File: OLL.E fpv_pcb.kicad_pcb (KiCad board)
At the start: 2 copper layers, 122 parts, among them J10 Conn_01x05_Pin, J2 RC, J3 Conn_01x02_Pin, J7 m4 rear left, J8 reciver, J9 TYPE-C-31-M-12, M1 M1 front left, M2 M2 front right, M3 M3 rear right, Q1 2N7002, U1 MP2315GJ, U10 AON7410, U11 UCC27511ADBV, U12 AON7410, U13 BMP280, U14 STM32H753VITx, U15 USBLC6-2SC6, U2 W25Q128JVSIQ, U3 MP2315GJ, U4 ICM-42688-P, U5 UCC27511ADBV, U6 ul_AON7410, U7 UCC27511ADBV, U8 AON7410, U9 UCC27511ADBV, Y2 8HMz

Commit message: update sd card
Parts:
- removed C13: 100nf, Capacitor_SMD:C_0603_1608Metric
- removed R7: 10k, Resistor_SMD:R_0603_1608Metric
- removed U2: W25Q128JVSIQ, Package_SO:SOIC-8-1EP_3.9x4.9mm_P1.27mm_EP2.29x3mm
- added C47: 100nF, Capacitor_SMD:C_0603_1608Metric, B.Cu at (253.1, 64.9)
- added C48: 10uF, Capacitor_SMD:C_0603_1608Metric, B.Cu at (251.3, 61.4)
- added J1: Micro_SD_Card, Connector_Card:microSD_HC_Hirose_DM3D-SF, B.Cu at (241.7, 69.7)
- added R28: 47k, Resistor_SMD:R_0603_1608Metric, B.Cu at (251.4, 67.5)
- added R29: 47k, Resistor_SMD:R_0603_1608Metric, B.Cu at (249.6, 67.4)
- added R30: 47k, Resistor_SMD:R_0603_1608Metric, B.Cu at (249.6, 64.3)
- added R31: 47k, Resistor_SMD:R_0603_1608Metric, B.Cu at (253.1, 61.4)
- added R32: 47k, Resistor_SMD:R_0603_1608Metric, B.Cu at (250.2, 69.8)
- added REF**: WEEE-Logo_4.2x6mm_SilkScreen, Symbol:WEEE-Logo_4.2x6mm_SilkScreen, F.Cu at (251.9, 43.3)
- added REF**: LayerMarker_2_3.81x2.54mm_TextH1mm_P1.27mm_Named, Symbol:LayerMarker_2_3.81x2.54mm_TextH1mm_P1.27mm_Named, F.Cu at (246.8, 43.3)
- added REF**: OSHW-Symbol_6.7x6mm_SilkScreen, Symbol:OSHW-Symbol_6.7x6mm_SilkScreen, B.Cu at (229.5, 55.0)
- D8, LS1: moved to B.Cu
- moved R27 102.0 mm to (253.1, 61.6), turned to 90 degrees
- moved R26 101.8 mm to (253.0, 58.4), turned to 90 degrees
- moved Q1 96.8 mm to (251.5, 65.1)
- moved D7 93.1 mm to (251.4, 68.4)
- moved LS1 81.2 mm to (228.2, 68.5), turned to 180 degrees
- moved C46 72.4 mm to (211.3, 56.7), turned to 90 degrees
- moved R24 72.4 mm to (224.3, 44.0), turned to 180 degrees
- moved C45 69.7 mm to (208.4, 56.0), turned to 180 degrees
- moved J9 63.9 mm to (209.7, 46.4), turned to -90 degrees
- moved R23 61.2 mm to (213.2, 40.4)
- moved D8 45.8 mm to (210.4, 53.4), turned to 180 degrees
- moved U15 45.8 mm to (209.1, 53.4)
- moved D6 41.5 mm to (219.7, 68.1), turned to 90 degrees
- moved M2 35.5 mm to (208.5, 59.2)
- moved U11 31.4 mm to (214.6, 68.6)
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- renumbered J7 to M2, M2 to M3, M3 to M4, J3 to j3
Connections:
- D6 pad 1: (no net) -> +VBAT
- D6 pad 2: (no net) -> Net-(C29--)
- LS1 pad 1: (no net) -> +5V_FC
- LS1 pad 2: (no net) -> GND
- U14 pad 51: CS_FLASH -> unconnected-(U14-PB12-Pad51)
- U14 pad 65: unconnected-(U14-PC8-Pad65) -> C1_D0
- U14 pad 66: unconnected-(U14-PC9-Pad66) -> C1_D1
- U14 pad 78: unconnected-(U14-PC10-Pad78) -> C1_D2
- U14 pad 79: unconnected-(U14-PC11-Pad79) -> C1_D3
- U14 pad 80: unconnected-(U14-PC12-Pad80) -> CLK
- U14 pad 83: unconnected-(U14-PD2-Pad83) -> CMD
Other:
- board outline added: 47.6 x 41.5 mm

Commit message: update IMU
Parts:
- removed JP1: Jumper_2_Open, Jumper:SolderJumper-2_P1.3mm_Open_RoundedPad1.0x1.5mm
- added SW1: SW_SPST, Button_Switch_SMD:SW_SPST_B3U-1000P, F.Cu at (243.3, 41.1)
- added SW2: SW_SPST, Button_Switch_SMD:SW_SPST_B3U-1000P, F.Cu at (246.9, 41.1)
- moved REF** 4.20 mm to (250.9, 42.9), turned to 90 degrees
- moved J1 0.77 mm to (241.2, 70.2)
- moved D8 0.64 mm to (210.8, 53.9)
- turned R5 to 180 degrees
- turned Y2 to 0 degrees
- renumbered j3 to BAT
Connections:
- D3 pad 1: +VBAT -> (no net)
- D3 pad 2: Net-(C26--) -> (no net)
- D4 pad 1: +VBAT -> (no net)
- D4 pad 2: Net-(C27--) -> (no net)
- D5 pad 1: +VBAT -> (no net)
- D5 pad 2: Net-(C28--) -> (no net)
- D6 pad 1: +VBAT -> (no net)
- D6 pad 2: Net-(C29--) -> (no net)
- LS1 pad 1: +5V_FC -> (no net)
- LS1 pad 2: GND -> (no net)
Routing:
- net GND: track 0.00 -> 75.3 mm, vias 0 -> 7
- net +VBAT: track 0.00 -> 56.9 mm, vias 0 -> 5
- net +3V3_FC: track 0.00 -> 21.2 mm, vias 0 -> 3
- net VDDA_FILT: track 0.00 -> 13.1 mm
- net Net-(C43-+): track 0.00 -> 12.8 mm, vias 0 -> 2
- net Net-(C42-+): track 0.00 -> 9.72 mm, vias 0 -> 2
- net GYRO_INT: track 0.00 -> 9.60 mm
- net BOOT0: track 0.00 -> 9.35 mm
- net ADC_VBAT: track 0.00 -> 9.10 mm
- net Net-(C18--): track 0.00 -> 9.08 mm, vias 0 -> 3
- net Net-(C19-+): track 0.00 -> 8.66 mm, vias 0 -> 2
- net Net-(R8-+): track 0.00 -> 7.97 mm
- net Net-(C18-+): track 0.00 -> 5.75 mm, vias 0 -> 2
- net SPI1_SDO: track 0.00 -> 3.95 mm
- net SPI1_SDI: track 0.00 -> 3.82 mm
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- added copper zone on F.Cu, net +3V3_FC
- added copper zone on F.Cu, net +3V3_IMU
- added copper zone on B.Cu, net GND
- added copper zone on F.Cu, net GND
- added copper zone on In1.Cu, net GND
- added copper zone on In4.Cu, net GND
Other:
- copper layers 2 -> 6

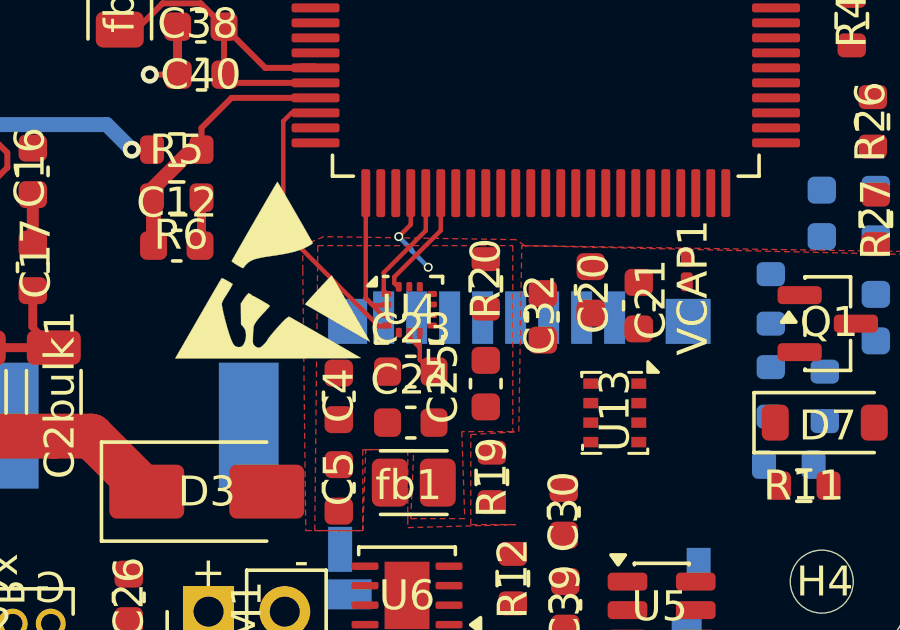
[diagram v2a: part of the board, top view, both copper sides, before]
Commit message: fix imu wire connection
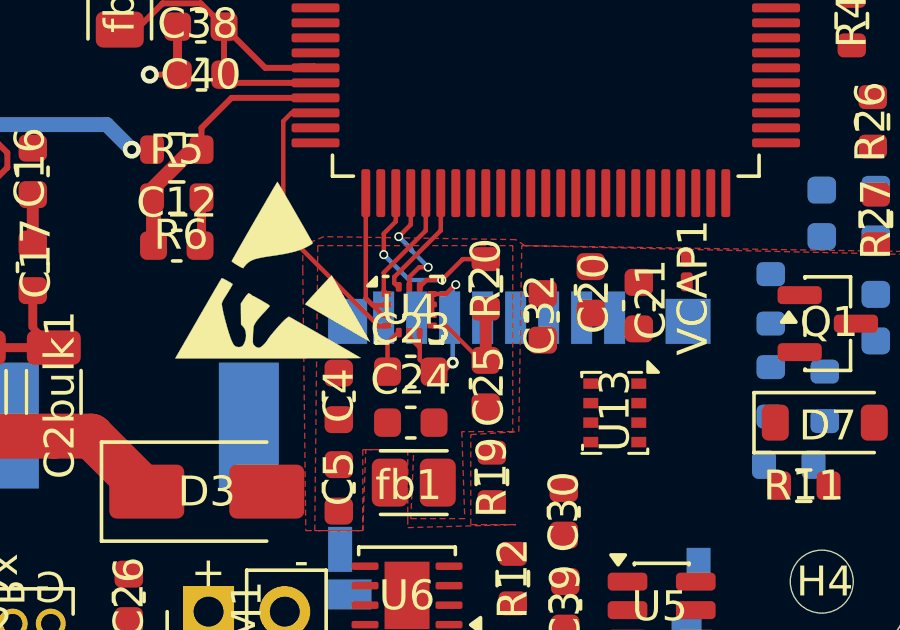
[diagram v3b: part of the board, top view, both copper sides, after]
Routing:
- net GYRO_CS: track 0.00 -> 7.07 mm, vias 0 -> 2
- net +3V3_IMU: track 0.00 -> 5.44 mm
- net GND: track 75.3 -> 80.2 mm, vias 7 -> 9
- net SPI1_SCK: track 3.04 -> 4.14 mm
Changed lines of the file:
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@@
 		(tags "capacitor")
 		(property "Reference" "C25"
-			(at 0 -1.43 90)
+			(at -0.1 0.1 90)
 			(layer "F.SilkS")
 			(effects
@@
 	)
 	(segment
+		(start 238.375 66.7)
+		(end 238.7 66.7)
+		(width 0.15)
+		(layer "F.Cu")
+		(net 1)
+	)
+	(segment
 		(start 220.8 63.5)
 		(end 222.3 65)
@@
 	)
 	(segment
+		(start 238.3125 64.1125)
+		(end 238.3125 64.7875)
+		(width 0.15)
+		(layer "F.Cu")
+		(net 1)
+	)
+	(segment
 		(start 226.5 47.3)
 		(end 226.5 46.5)
@@
 	)
 	(segment
+		(start 238.7 66.7)
+		(end 239 66.4)
+		(width 0.15)
+		(layer "F.Cu")
+		(net 1)
+	)
+	(segment
 		(start 237.9 66.3)
 		(end 237.9 65.9)
@@
 	)
 	(segment
+		(start 238.769671 64.1125)
+		(end 239.041086 63.841085)
+		(width 0.15)
+		(layer "F.Cu")
+		(net 1)
+	)
+	(segment
 		(start 236.6 43.675)
 		(end 236.6 45.4)
@@
 	)
 	(segment
+		(start 238.3125 64.1125)
+		(end 238.769671 64.1125)
+		(width 0.15)
+		(layer "F.Cu")
+		(net 1)
+	)
+	(segment
 		(start 236.633968 64.7875)
 		(end 236.7875 64.7875)
@@
 	)
 	(via
+		(at 239 66.4)
+		(size 0.4)
+		(drill 0.2)
+		(layers "F.Cu" "B.Cu")
+		(net 1)
+	)
+	(via
 		(at 226.5 46.5)
 		(size 0.6)
@@
 	)
 	(via
+		(at 239.1 63.8)
+		(size 0.3)
+		(drill 0.2)
+		(layers "F.Cu" "B.Cu")
+		(net 1)
+	)
+	(via
 		(at 226.2 39.9)
 		(size 0.6)
@@
 	)
 	(segment
+		(start 239 66.4)
+		(end 239 63.9)
+		(width 0.15)
+		(layer "B.Cu")
+		(net 1)
+	)
+	(segment
 		(start 226.2 39.9)
 		(end 225.4 39.9)
@@
 	)
 	(segment
+		(start 239 63.9)
+		(end 239.1 63.8)
+		(width 0.15)
+		(layer "B.Cu")
+		(net 1)
+	)
+	(segment
 		(start 221.5 65.8)
 		(end 222.3 65)
@@
 	)
 	(segment
+		(start 240.1 66.325)
+		(end 239.925 66.325)
+		(width 0.4)
+		(layer "F.Cu")
+		(net 4)
+	)
+	(segment
+		(start 238.35 65.2)
+		(end 238.3125 65.1625)
+		(width 0.1)
+		(layer "F.Cu")
+		(net 4)
+	)
+	(segment
+		(start 238.8 65.2)
+		(end 238.35 65.2)
+		(width 0.14)
+		(layer "F.Cu")
+		(net 4)
+	)
+	(segment
+		(start 240.1 64.6)
+		(end 240.1 66.325)
+		(width 0.4)
+		(layer "F.Cu")
+		(net 4)
+	)
+	(segment
+		(start 236.825 66.7)
+		(end 236.825 65.75)
+		(width 0.15)
+		(layer "F.Cu")
+		(net 4)
+	)
+	(segment
+		(start 239.925 66.325)
+		(end 238.8 65.2)
+		(width 0.14)
+		(layer "F.Cu")
+		(net 4)
+	)
+	(segment
+		(start 236.825 65.75)
+		(end 237.175 65.4)
+		(width 0.15)
+		(layer "F.Cu")
+		(net 4)
+	)
+	(segment
 		(start 231.625 57.575)
 		(end 234.425 57.575)
@@
 	)
 	(segment
+		(start 239.33113 62.95)
+		(end 240.1 62.95)
+		(width 0.15)
+		(layer "F.Cu")
+		(net 55)
+	)
+	(segment
+		(start 237.925 63.85)
+		(end 237.925 63.875)
+		(width 0.15)
+		(layer "F.Cu")
+		(net 55)
+	)
+	(segment
+		(start 237.1 60.75)
+		(end 237.1 61.698959)
+		(width 0.15)
+		(layer "F.Cu")
+		(net 55)
+	)
+	(segment
+		(start 238.635269 63.645861)
+		(end 238.129139 63.645861)
+		(width 0.15)
+		(layer "F.Cu")
+		(net 55)
+	)
+	(segment
+		(start 238.129139 63.645861)
+		(end 237.925 63.85)
+		(width 0.15)
+		(layer "F.Cu")
+		(net 55)
+	)
+	(segment
+		(start 238.635269 63.645861)
+		(end 239.33113 62.95)
+		(width 0.15)
+		(layer "F.Cu")
+		(net 55)
+	)
+	(segment
+		(start 237.1 61.698959)
+		(end 236.7 62.098959)
+		(width 0.15)
+		(layer "F.Cu")
+		(net 55)
+	)
+	(segment
+		(start 236.7 62.098959)
+		(end 236.7 62.8)
+		(width 0.15)
+		(layer "F.Cu")
+		(net 55)
+	)
+	(via
+		(at 238.635269 63.645861)
+		(size 0.3)
+		(drill 0.2)
+		(layers "F.Cu" "B.Cu")
+		(net 55)
+	)
+	(via
+		(at 236.7 62.8)
+		(size 0.3)
+		(drill 0.2)
+		(layers "F.Cu" "B.Cu")
+		(net 55)
+	)
+	(segment
+		(start 237.545861 63.645861)
+		(end 236.7 62.8)
+		(width 0.15)
+		(layer "B.Cu")
+		(net 55)
+	)
+	(segment
+		(start 238.635269 63.645861)
+		(end 237.545861 63.645861)
+		(width 0.15)
+		(layer "B.Cu")
+		(net 55)
+	)
+	(segment
 		(start 238.1 62)
 		(end 236.7 63.4)
@@
 	)
 	(segment
+		(start 237.879139 63.220861)
+		(end 237.55 63.55)
+		(width 0.15)
+		(layer "F.Cu")
+		(net 61)
+	)
+	(segment
+		(start 237.55 63.55)
+		(end 237.55 63.875)
+		(width 0.15)
+		(layer "F.Cu")
+		(net 61)
+	)
+	(segment
+		(start 238.181675 63.220861)
+		(end 237.879139 63.220861)
+		(width 0.15)
+		(layer "F.Cu")
+		(net 61)
+	)
+	(segment
 		(start 237.6 61.8)
 		(end 237.6 60.75)
@@
 	)
 	(segment
-		(start 237.613553 62.652739)
-		(end 238.181675 63.220861)
+		(start 237.2 62.2)
+		(end 237.613553 62.613553)
 		(width 0.15)
 		(layer "B.Cu")
@@
 	)
 	(segment
-		(start 237.2 62.2)
-		(end 237.613553 62.613553)
+		(start 237.613553 62.613553)
+		(end 237.613553 62.652739)
 		(width 0.15)
 		(layer "B.Cu")
@@
 	)
 	(segment
-		(start 237.613553 62.613553)
-		(end 237.613553 62.652739)
+		(start 237.613553 62.652739)
+		(end 238.181675 63.220861)
 		(width 0.15)
 		(layer "B.Cu")
@@
 	)
 	(segment
-		(start 238.6 61.994974)
-		(end 237.05 63.544974)
+		(start 237.05 63.75)
+		(end 237.175 63.875)
 		(width 0.15)
 		(layer "F.Cu")
@@
 	)
 	(segment
-		(start 238.6 60.75)
-		(end 238.6 61.994974)
+		(start 238.6 61.994974)
+		(end 237.05 63.544974)
 		(width 0.15)
 		(layer "F.Cu")
@@
 	)
 	(segment
-		(start 237.05 63.75)
-		(end 237.175 63.875)
+		(start 237.05 63.544974)
+		(end 237.05 63.75)
 		(width 0.15)
 		(layer "F.Cu")
@@
 	)
 	(segment
-		(start 237.05 63.544974)
-		(end 237.05 63.75)
+		(start 238.6 60.75)
+		(end 238.6 61.994974)
 		(width 0.15)
 		(layer "F.Cu")
